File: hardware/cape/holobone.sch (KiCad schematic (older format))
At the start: 64 parts, among them J1 Conn_01x03, J3 Conn_01x03, J4 Conn_01x03, P1 BeagleBone_Black_Header, P2 BeagleBone_Black_Header, SW1 SW_DIP_x02, U1 LM4040DBZ-2.0, U2 CAT24C256, U3 TL084, U4 TL084, U5 MCP4922-EST, U6 ST1S50

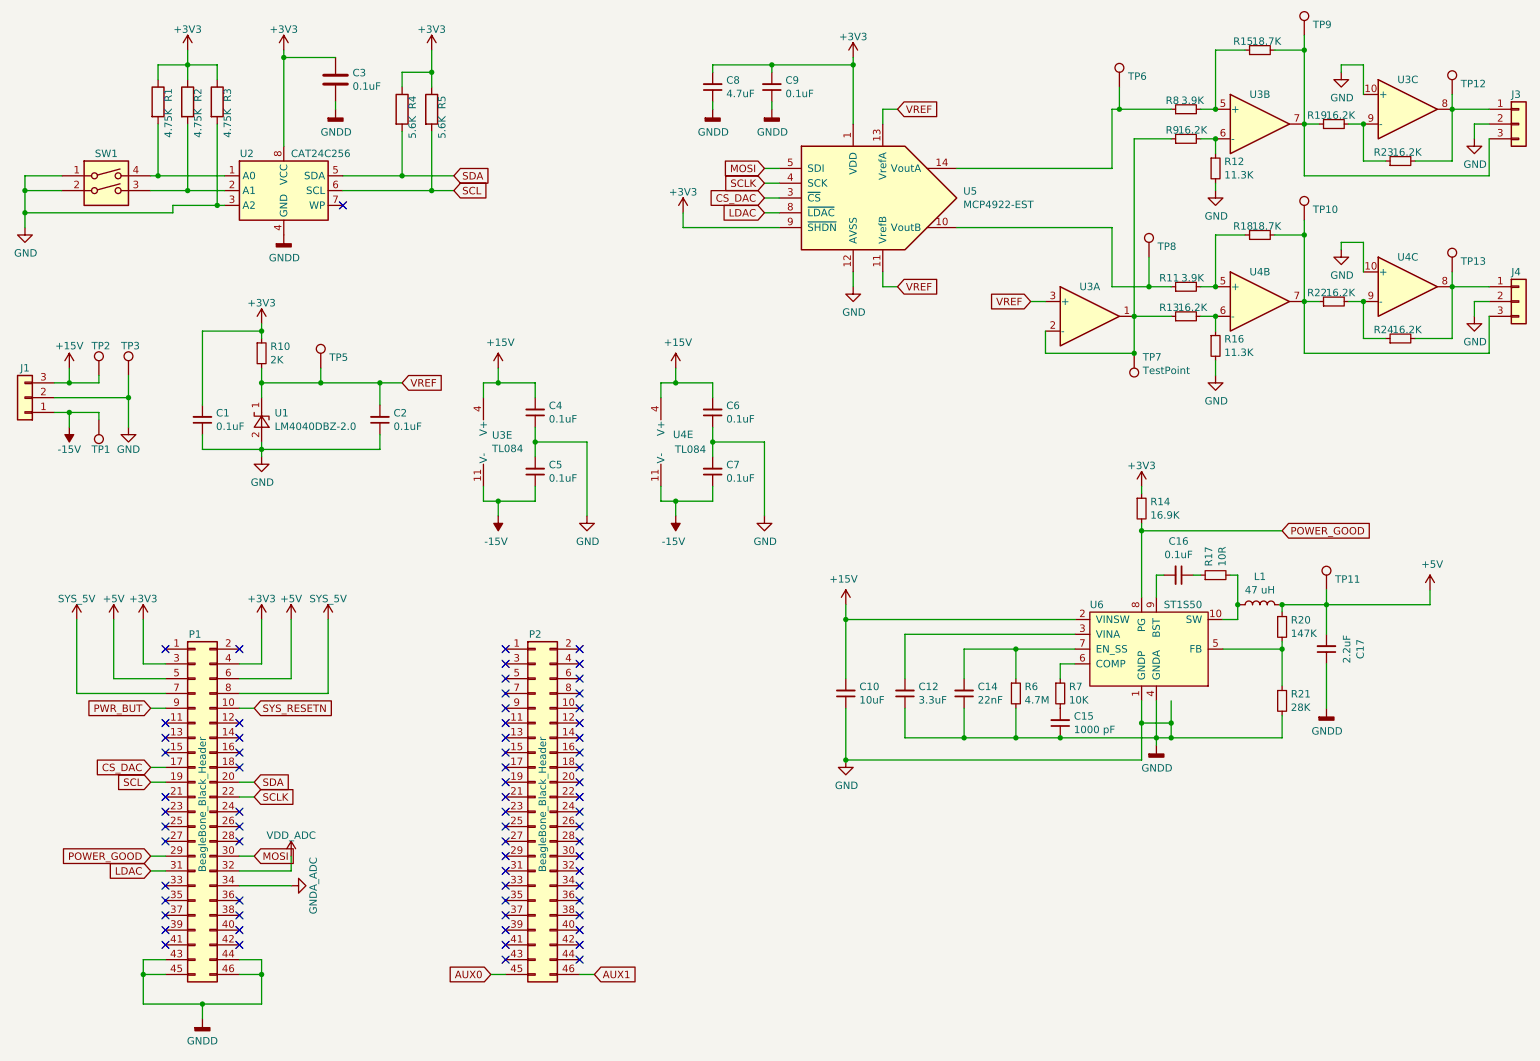
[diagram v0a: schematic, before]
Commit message: second hardware revision schematics done
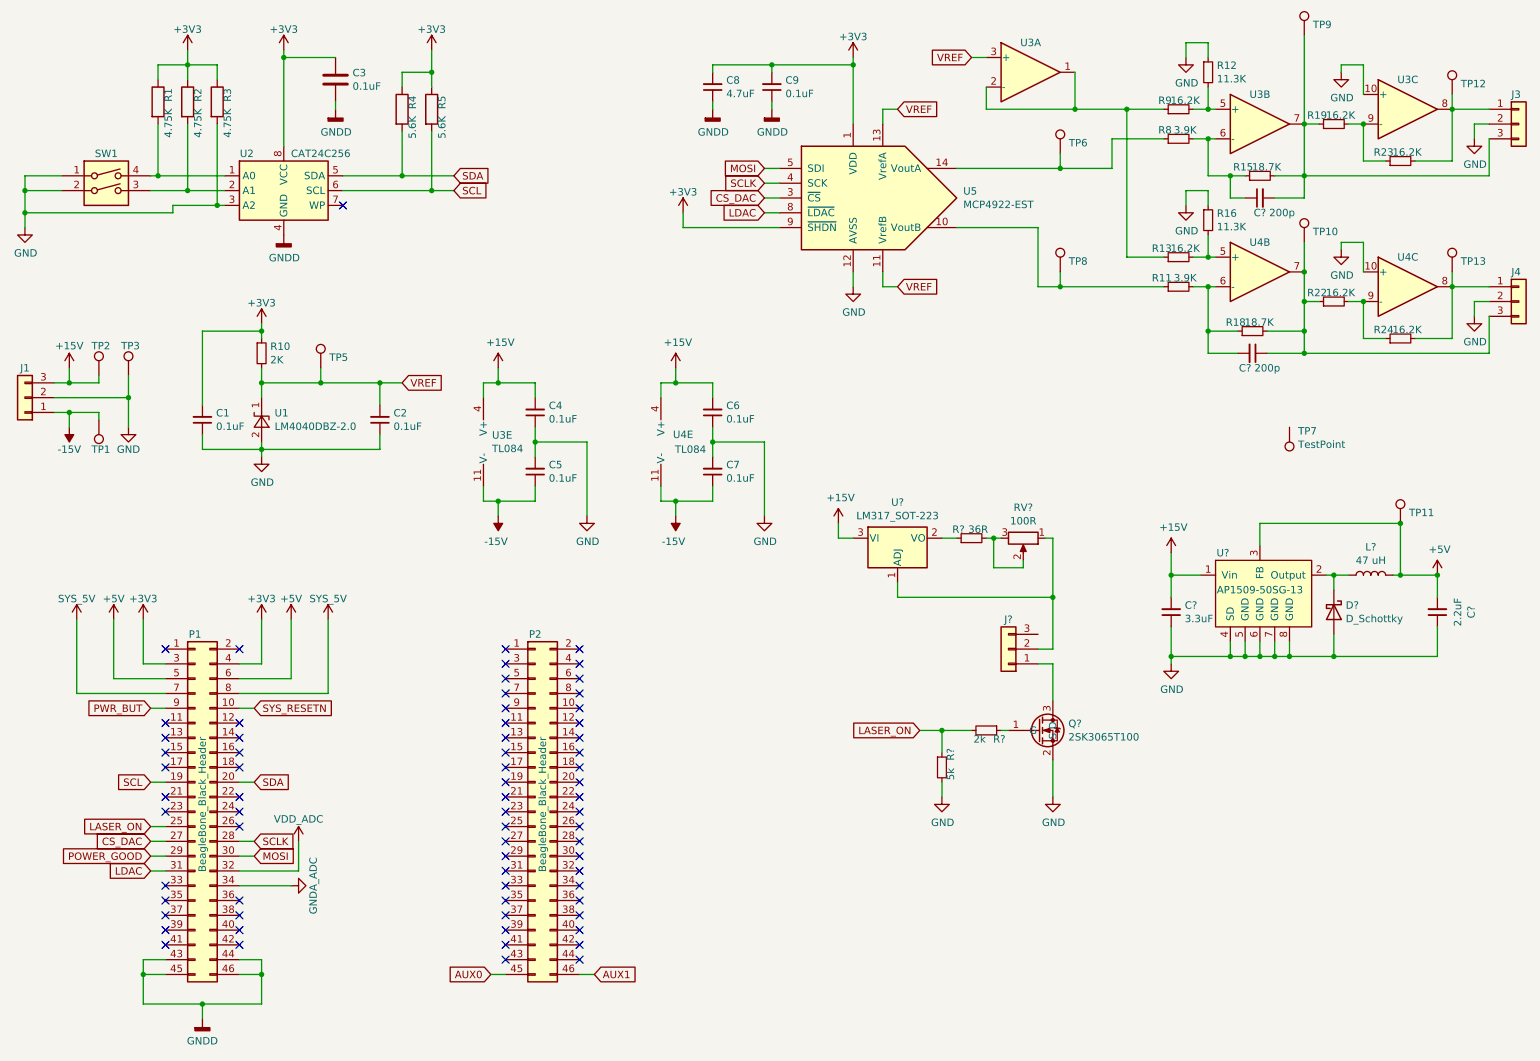
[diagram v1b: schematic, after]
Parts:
- removed C10: 10uF, Capacitor_SMD:C_0805_2012Metric, symbol Device:C_Small
- removed C12: 3.3uF, Capacitor_SMD:C_0805_2012Metric, symbol Device:C_Small
- removed C14: 22nF, Capacitor_SMD:C_0805_2012Metric, symbol Device:C_Small
- removed C15: 1000 pF, Capacitor_SMD:C_0805_2012Metric, symbol Device:C_Small
- removed C16: 0.1uF, Capacitor_SMD:C_0805_2012Metric, symbol Device:C_Small
- removed C17: 2.2uF, Capacitor_SMD:C_0805_2012Metric, symbol Device:C_Small
- removed L1: 47 uH, Inductor_SMD:L_12x12mm_H8mm, symbol Device:L
- removed R14: 16.9K, Resistor_SMD:R_0805_2012Metric, symbol Device:R_Small
- removed R17: 10R, Resistor_SMD:R_0805_2012Metric, symbol Device:R_Small
- removed R20: 147K, Resistor_SMD:R_0805_2012Metric, symbol Device:R_Small
- removed R21: 28K, Resistor_SMD:R_0805_2012Metric, symbol Device:R_Small
- removed R6: 4.7M, Resistor_SMD:R_0805_2012Metric, symbol Device:R_Small
- removed R7: 10K, Resistor_SMD:R_0805_2012Metric, symbol Device:R_Small
- removed U6: ST1S50, Package_DFN_QFN:DFN-10-1EP_3x3mm_P0.5mm_EP1.65x2.38mm, symbol holobone:ST1S50
- added C?: 3.3uF, Capacitor_SMD:C_0805_2012Metric, symbol Device:C_Small
- added C?: 2.2uF, Capacitor_SMD:C_0805_2012Metric, symbol Device:C_Small
- added C? (x2): 200p, Capacitor_SMD:C_0805_2012Metric_Pad1.15x1.40mm_HandSolder, symbol Device:C_Small
- added D?: D_Schottky, Diode_SMD:D_SOD-123, symbol Device:D_Schottky
- added J?: Conn_01x03, Connector_JST:JST_XH_S3B-XH-A-1_1x03_P2.50mm_Horizontal, symbol Connector_Generic:Conn_01x03
- added L?: 47 uH, Inductor_SMD:L_12x12mm_H8mm, symbol Device:L
- added Q?: 2SK3065T100, Package_TO_SOT_SMD:SOT-89-3_Handsoldering, symbol holobone:2SK3065T100
- added R?: 36R, Resistor_SMD:R_0805_2012Metric, symbol Device:R_Small
- added R?: 5k, Resistor_SMD:R_0805_2012Metric, symbol Device:R_Small
- added R?: 2k, Resistor_SMD:R_0805_2012Metric, symbol Device:R_Small
- added RV?: 100R, Potentiometer_THT:Potentiometer_Bourns_3296W_Vertical, symbol Device:R_POT
- added U?: AP1509-50SG-13, Package_SO:SOP-8_3.76x4.96mm_P1.27mm, symbol holobone:AP1509-50SG-13
- added U?: LM317_SOT-223, Package_TO_SOT_SMD:SOT-223-3_TabPin2, symbol Regulator_Linear:LM317_SOT-223
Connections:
- net +15V: now also C?.2, U?.1 (Vin), U?.3 (VI)
- net +5V: now also C?.2, L?.2, U?.3 (FB)
- net CS_DAC: now also P1.27 (Pin_27); no longer P1.17 (Pin_17)
- net GND: now also R12.1, R16.1, C?.1, C?.1, D?.2 (A), Q?.2 (S), R?.2, U?.4 (SD), U?.5 (GND), U?.6 (GND), U?.7 (GND), U?.8 (GND); no longer C3.2, C8.1, C9.1, P1.43 (Pin_43), P1.44 (Pin_44), P1.45 (Pin_45), P1.46 (Pin_46), R12.2, R16.2, U2.4 (GND)
- net SCLK: now also P1.28 (Pin_28); no longer P1.22 (Pin_22)
- net LASER_ON: now reaches P1.25 (Pin_25)
- net LASER_ON: now also R?.1, R?.2
- net at R13.1, R9.1, U3.1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: no longer TP7.1
- net at R11.2, R18.1: now also U4.6 (-), C?.2; no longer U4.5 (+)
- net at J4.3 (Pin_3), R18.2, R22.1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: now also C?.1
- net at R15.1, R8.2: now also U3.6 (-), C?.1; no longer U3.5 (+)
- net at J3.3 (Pin_3), R15.2, R19.1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: now also C?.2
- new net: R13.2, R16.2, U4.5 (+)
- new net: R12.2, R9.2, U3.5 (+)
- new net: Q?.1 (G), R?.1
- new net: J?.1 (Pin_1), Q?.3 (D)
- new net: D?.1 (K), L?.1, U?.2 (Output)
- new net: J?.2 (Pin_2), RV?.1, U?.1 (ADJ)
- new net: R?.1, U?.2 (VO)
- new net: R?.2, RV?.2, RV?.3
- new net GNDD: C3.2, C8.1, C9.1, P1.43 (Pin_43), P1.44 (Pin_44), P1.45 (Pin_45), P1.46 (Pin_46), U2.4 (GND)
- no-connect marks 70 -> 69
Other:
- moved on the sheet: R11, R12, R13, R15, R16, R18, R8, R9, TP10, TP11, TP6, TP7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

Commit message: Minor changes
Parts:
- gave numbers to parts that had none: 14
- renumbered C3 to C2, C2 to C3, C8 to C6, C6 to C7, C7 to C8, R9 to R10, R8 to R11, R13 to R12, R11 to R13, R12 to R14, R16 to R15, R18 to R16, R15 to R17, R19 to R18, R22 to R19, R23 to R20, R24 to R21, R10 to R4, R4 to R5, R5 to R6, TP2 to TP1, TP11 to TP10, TP12 to TP11, TP13 to TP12, TP1 to TP2, TP5 to TP4, TP6 to TP5, TP8 to TP6, TP9 to TP8, TP10 to TP9
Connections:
- net GNDD is gone; now on net GND: C2.2, C6.1, C9.1, P1.43 (Pin_43), P1.44 (Pin_44), P1.45 (Pin_45), P1.46 (Pin_46), U2.4 (GND)
- net GNDA_ADC: no longer names the net of P1.34 (Pin_34)
- net VDD_ADC: no longer names the net of P1.32 (Pin_32)
- no-connect marks 69 -> 71
